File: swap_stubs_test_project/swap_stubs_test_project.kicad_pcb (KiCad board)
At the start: 2 copper layers, 2 parts, among them U101 74LVC541, U102 74LVC541

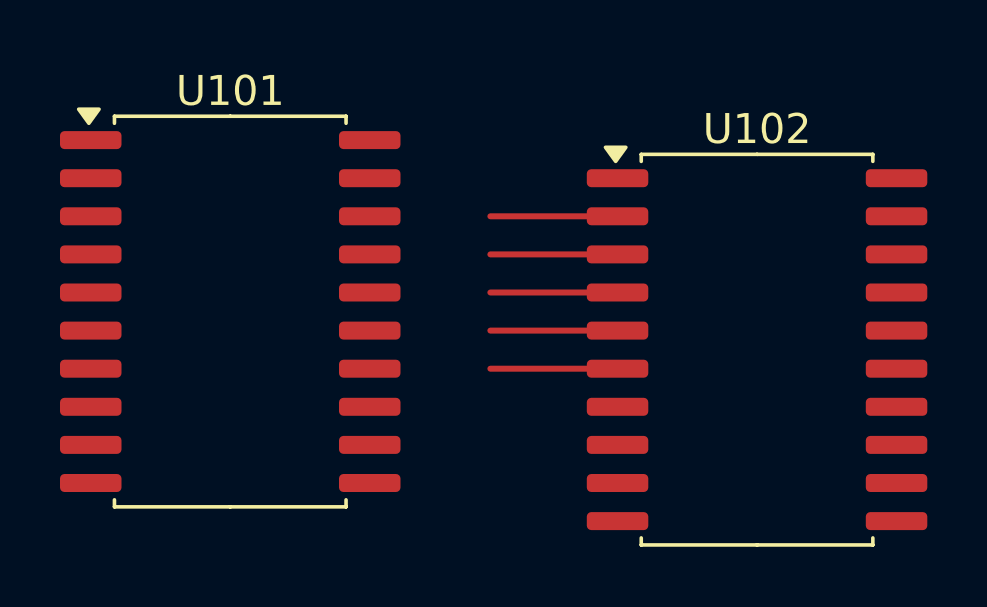
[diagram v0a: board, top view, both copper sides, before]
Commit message: support global and hierarchical labels also
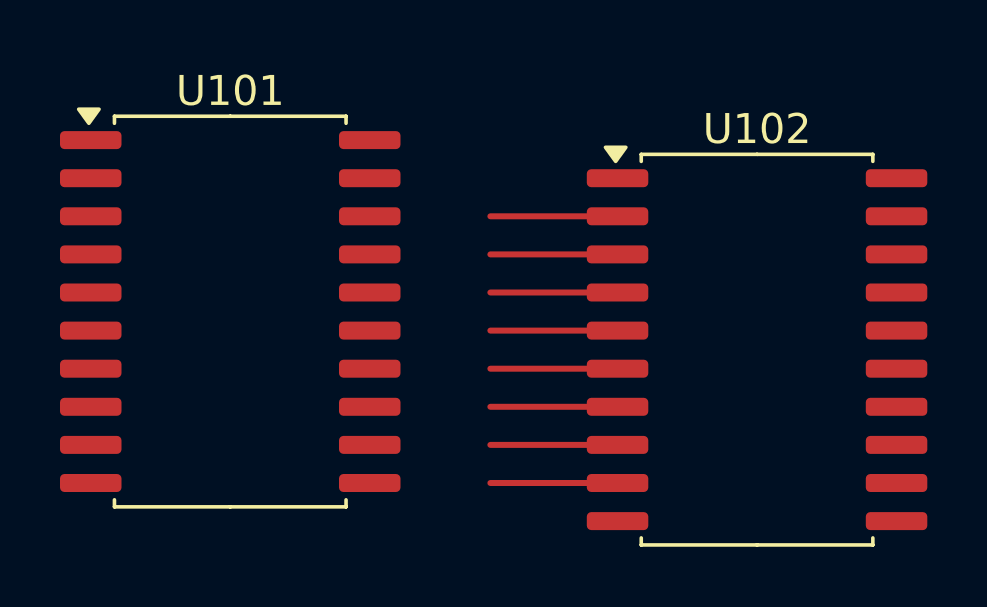
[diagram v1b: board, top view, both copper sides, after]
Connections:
- U101 pad 11: /label8 -> /label7
- U101 pad 12: /label7 -> label8
- U101 pad 13: /label6 -> /label5
- U101 pad 14: /label5 -> /label6
- U101 pad 15: /label4 -> label3
- U101 pad 16: /label3 -> label4
- U101 pad 17: /label2 -> /label1
- U101 pad 18: /label1 -> /label2
- U102 pad 2: /label8 -> /label1
- U102 pad 3: /label7 -> /label2
- U102 pad 4: /label6 -> label3
- U102 pad 5: /label5 -> label4
- U102 pad 6: /label4 -> /label5
- U102 pad 7: /label3 -> /label6
- U102 pad 8: /label2 -> /label7
- U102 pad 9: /label1 -> label8
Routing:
- net label8: track 0.00 -> 4.24 mm
- net label4: track 0.00 -> 4.24 mm
- net label3: track 0.00 -> 4.24 mm
- net /label8: track 4.24 -> 0.00 mm
- net /label4: track 4.24 -> 0.00 mm
- net /label2: track 0.00 -> 4.24 mm
- net /label1: track 0.00 -> 4.24 mm
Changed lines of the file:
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@@
 	(net 3 "unconnected-(U101-A7-Pad9)")
 	(net 4 "unconnected-(U101-A3-Pad5)")
-	(net 5 "/label8")
+	(net 5 "/label7")
 	(net 6 "unconnected-(U101-A2-Pad4)")
 	(net 7 "/label1")
 	(net 8 "GND")
-	(net 9 "/label7")
+	(net 9 "label8")
 	(net 10 "/label5")
-	(net 11 "/label4")
+	(net 11 "label3")
 	(net 12 "unconnected-(U101-A4-Pad6)")
 	(net 13 "unconnected-(U101-A1-Pad3)")
@@
 	(net 17 "+3V3")
 	(net 18 "Net-(U101-G2)")
-	(net 19 "/label3")
+	(net 19 "label4")
 	(net 20 "/label2")
 	(net 21 "unconnected-(U102-Y1-Pad17)")
@@
 				(font
 					(size 1.27 1.27)
+					(thickness 0.15)
 				)
 			)
@@
 				(font
 					(size 1.27 1.27)
+					(thickness 0.15)
 				)
 			)
@@
 				(font
 					(size 1.27 1.27)
+					(thickness 0.15)
 				)
 			)
@@
 			(layers "F.Cu" "F.Paste" "F.Mask")
 			(roundrect_rratio 0.25)
-			(net 5 "/label8")
+			(net 7 "/label1")
 			(pinfunction "A0")
 			(pintype "input")
@@
 			(layers "F.Cu" "F.Paste" "F.Mask")
 			(roundrect_rratio 0.25)
-			(net 9 "/label7")
+			(net 20 "/label2")
 			(pinfunction "A1")
 			(pintype "input")
@@
 			(layers "F.Cu" "F.Paste" "F.Mask")
 			(roundrect_rratio 0.25)
-			(net 1 "/label6")
+			(net 11 "label3")
 			(pinfunction "A2")
 			(pintype "input")
@@
 			(layers "F.Cu" "F.Paste" "F.Mask")
 			(roundrect_rratio 0.25)
-			(net 10 "/label5")
+			(net 19 "label4")
 			(pinfunction "A3")
 			(pintype "input")
@@
 			(layers "F.Cu" "F.Paste" "F.Mask")
 			(roundrect_rratio 0.25)
-			(net 11 "/label4")
+			(net 10 "/label5")
 			(pinfunction "A4")
 			(pintype "input")
@@
 			(layers "F.Cu" "F.Paste" "F.Mask")
 			(roundrect_rratio 0.25)
-			(net 19 "/label3")
+			(net 1 "/label6")
 			(pinfunction "A5")
 			(pintype "input")
@@
 			(layers "F.Cu" "F.Paste" "F.Mask")
 			(roundrect_rratio 0.25)
-			(net 20 "/label2")
+			(net 5 "/label7")
 			(pinfunction "A6")
 			(pintype "input")
@@
 			(layers "F.Cu" "F.Paste" "F.Mask")
 			(roundrect_rratio 0.25)
-			(net 7 "/label1")
+			(net 9 "label8")
 			(pinfunction "A7")
 			(pintype "input")
@@
 				(font
 					(size 1.27 1.27)
+					(thickness 0.15)
 				)
 			)
@@
 				(font
 					(size 1.27 1.27)
+					(thickness 0.15)
 				)
 			)
@@
 				(font
 					(size 1.27 1.27)
+					(thickness 0.15)
 				)
 			)
@@
 			(layers "F.Cu" "F.Paste" "F.Mask")
 			(roundrect_rratio 0.25)
-			(net 5 "/label8")
+			(net 5 "/label7")
 			(pinfunction "Y7")
 			(pintype "tri_state")
@@
 			(layers "F.Cu" "F.Paste" "F.Mask")
 			(roundrect_rratio 0.25)
-			(net 9 "/label7")
+			(net 9 "label8")
 			(pinfunction "Y6")
 			(pintype "tri_state")
@@
 			(layers "F.Cu" "F.Paste" "F.Mask")
 			(roundrect_rratio 0.25)
-			(net 1 "/label6")
+			(net 10 "/label5")
 			(pinfunction "Y5")
 			(pintype "tri_state")
@@
 			(layers "F.Cu" "F.Paste" "F.Mask")
 			(roundrect_rratio 0.25)
-			(net 10 "/label5")
+			(net 1 "/label6")
 			(pinfunction "Y4")
 			(pintype "tri_state")
@@
 			(layers "F.Cu" "F.Paste" "F.Mask")
 			(roundrect_rratio 0.25)
-			(net 11 "/label4")
+			(net 11 "label3")
 			(pinfunction "Y3")
 			(pintype "tri_state")
@@
 			(layers "F.Cu" "F.Paste" "F.Mask")
 			(roundrect_rratio 0.25)
-			(net 19 "/label3")
+			(net 19 "label4")
 			(pinfunction "Y2")
 			(pintype "tri_state")
@@
 			(layers "F.Cu" "F.Paste" "F.Mask")
 			(roundrect_rratio 0.25)
-			(net 20 "/label2")
+			(net 7 "/label1")
 			(pinfunction "Y1")
 			(pintype "tri_state")
@@
 			(layers "F.Cu" "F.Paste" "F.Mask")
 			(roundrect_rratio 0.25)
-			(net 7 "/label1")
+			(net 20 "/label2")
 			(pinfunction "Y0")
 			(pintype "tri_state")
@@
 			)
 		)
+	)
+	(segment
+		(start 157.275 90.17)
+		(end 153.035 90.17)
+		(width 0.2)
+		(layer "F.Cu")
+		(net 1)
+	)
+	(segment
+		(start 157.275 91.44)
+		(end 153.035 91.44)
+		(width 0.2)
+		(layer "F.Cu")
+		(net 5)
+	)
+	(segment
+		(start 157.275 83.82)
+		(end 153.035 83.82)
+		(width 0.2)
+		(layer "F.Cu")
+		(net 7)
+	)
+	(segment
+		(start 157.275 92.71)
+		(end 153.035 92.71)
+		(width 0.2)
+		(layer "F.Cu")
+		(net 9)
+	)
+	(segment
+		(start 157.275 88.9)
+		(end 153.035 88.9)
+		(width 0.2)
+		(layer "F.Cu")
+		(net 10)
 	)
 	(segment
@@
 		(width 0.2)
 		(layer "F.Cu")
-		(net 1)
+		(net 11)
 	)
 	(segment
-		(start 157.275 83.82)
-		(end 153.035 83.82)
+		(start 157.275 87.63)
+		(end 153.035 87.63)
 		(width 0.2)
 		(layer "F.Cu")
-		(net 5)
+		(net 19)
 	)
 	(segment
@@
 		(width 0.2)
 		(layer "F.Cu")
-		(net 9)
-	)
-	(segment
-		(start 157.275 87.63)
-		(end 153.035 87.63)
-		(width 0.2)
-		(layer "F.Cu")
-		(net 10)
-	)
-	(segment
-		(start 157.275 88.9)
-		(end 153.035 88.9)
-		(width 0.2)
-		(layer "F.Cu")
-		(net 11)
+		(net 20)
 	)
 )
